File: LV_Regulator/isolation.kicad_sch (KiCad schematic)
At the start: 17 parts, among them IC1 UCC12040DVE, J1 430450800, J2 430450400, J3 430450800, J4 430450400, K1 41.52.9.005.0010, U1 ADM2483xRW

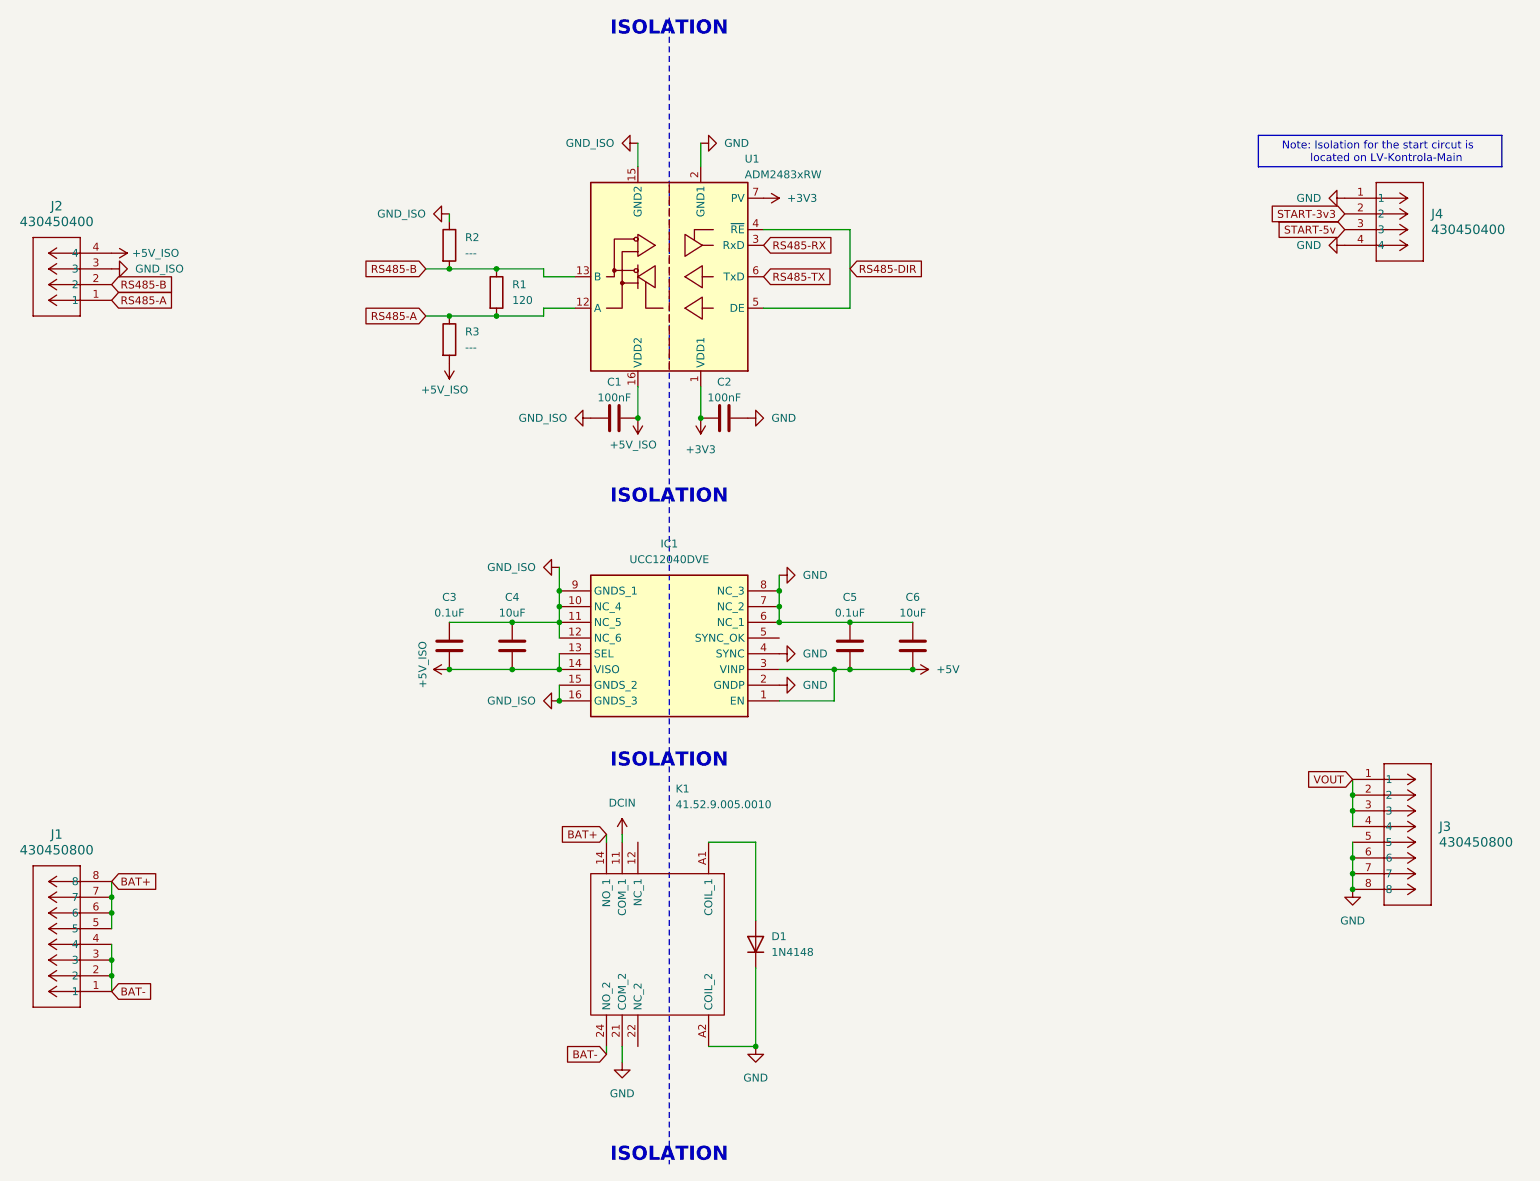
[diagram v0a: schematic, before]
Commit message: Added Start Control
Added Start Control MCU to the LV_Kontrola_Main, added hsc/lsc to LV_Regulator, fixed component numbering
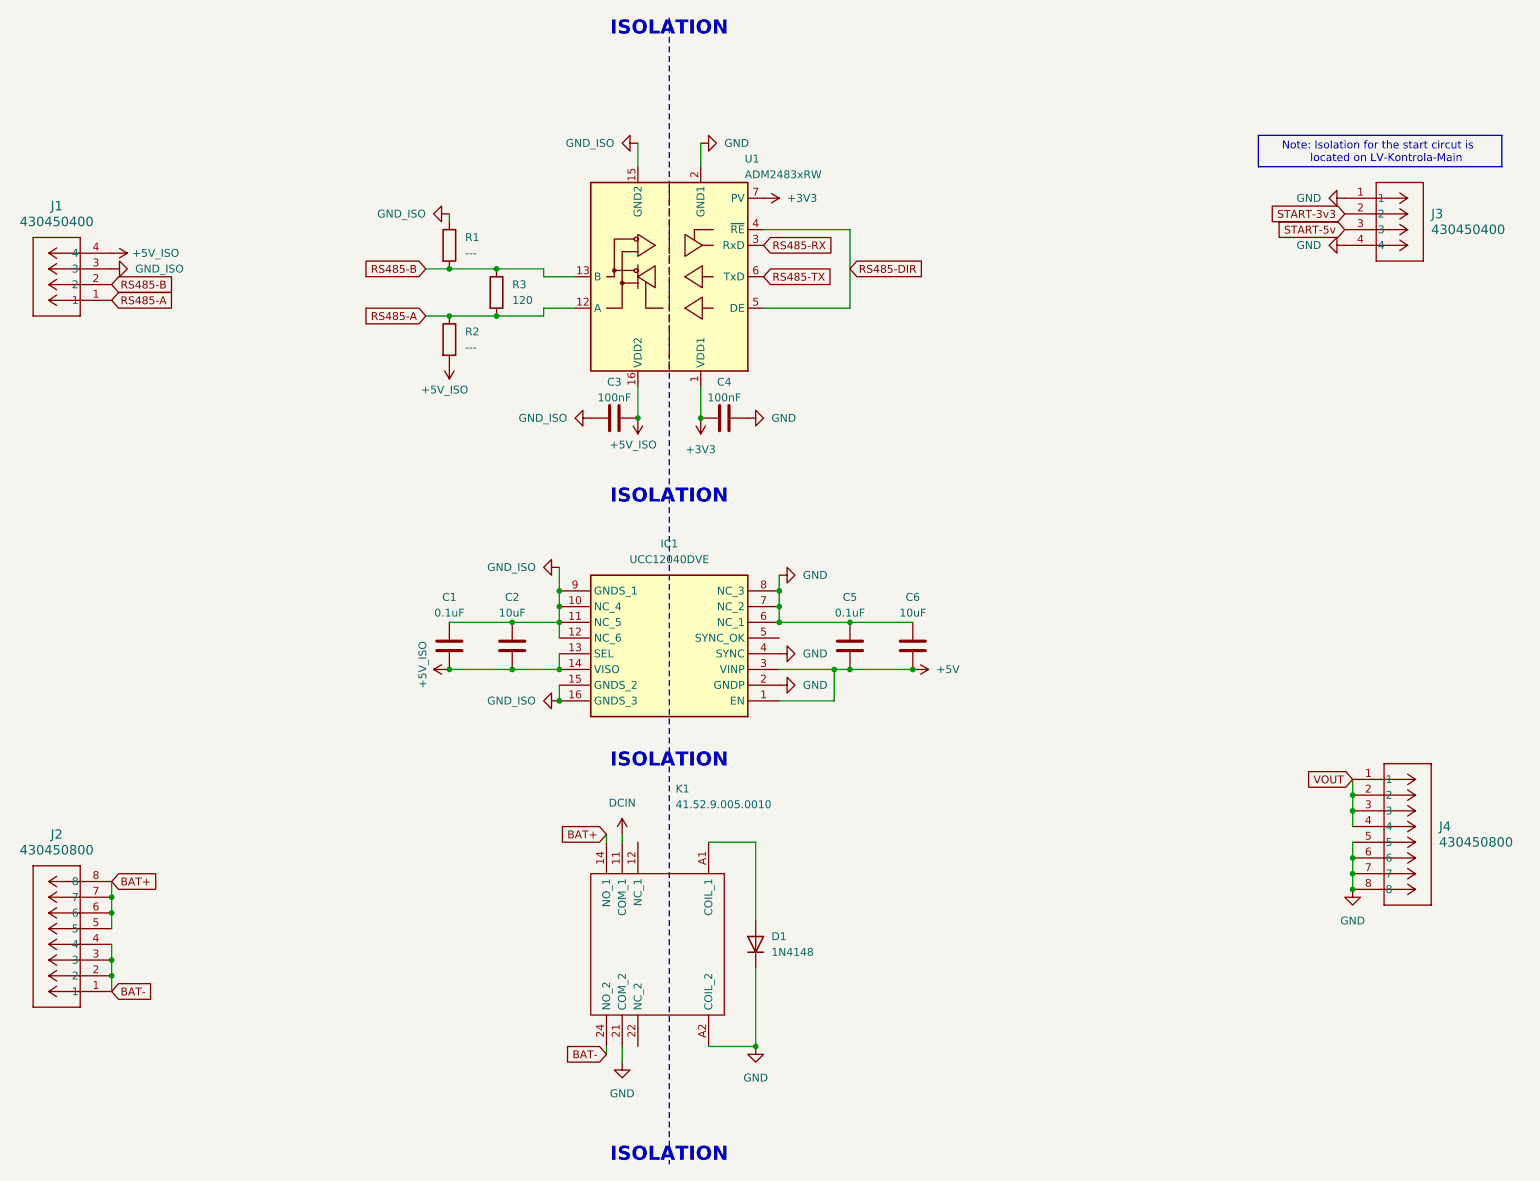
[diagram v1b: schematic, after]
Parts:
- renumbered C3 to C1, C4 to C2, C1 to C3, C2 to C4, J2 to J1, J1 to J2, J4 to J3, J3 to J4, R2 to R1, R3 to R2, R1 to R3

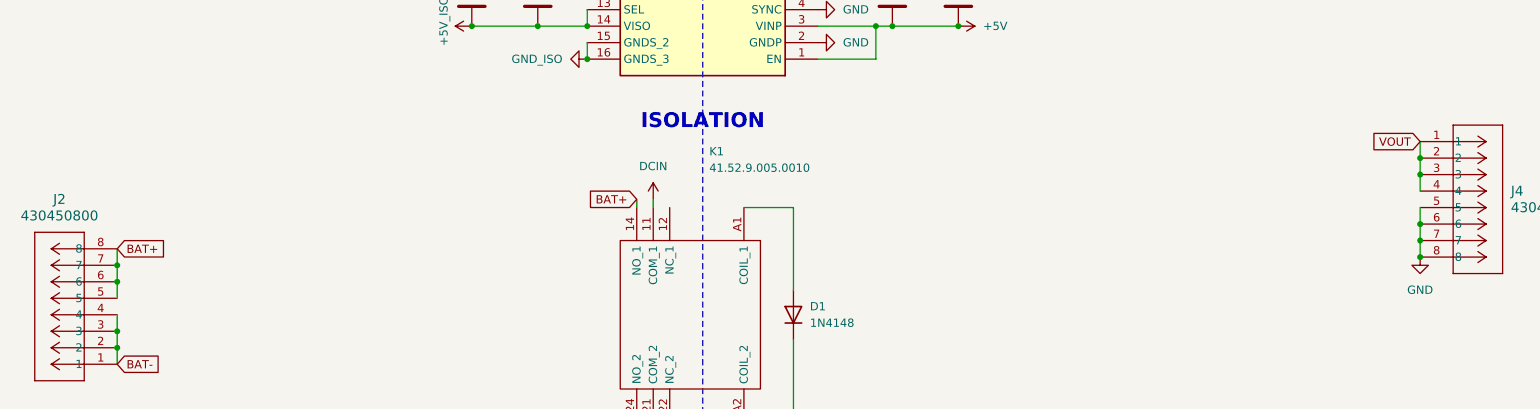
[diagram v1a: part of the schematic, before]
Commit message: Added Stat logic
Added start mcu and associated components to the LV_Kontrola_Main schematic, added STM32CubeIDE project and basic configuration, added fuses to LV_Regulator
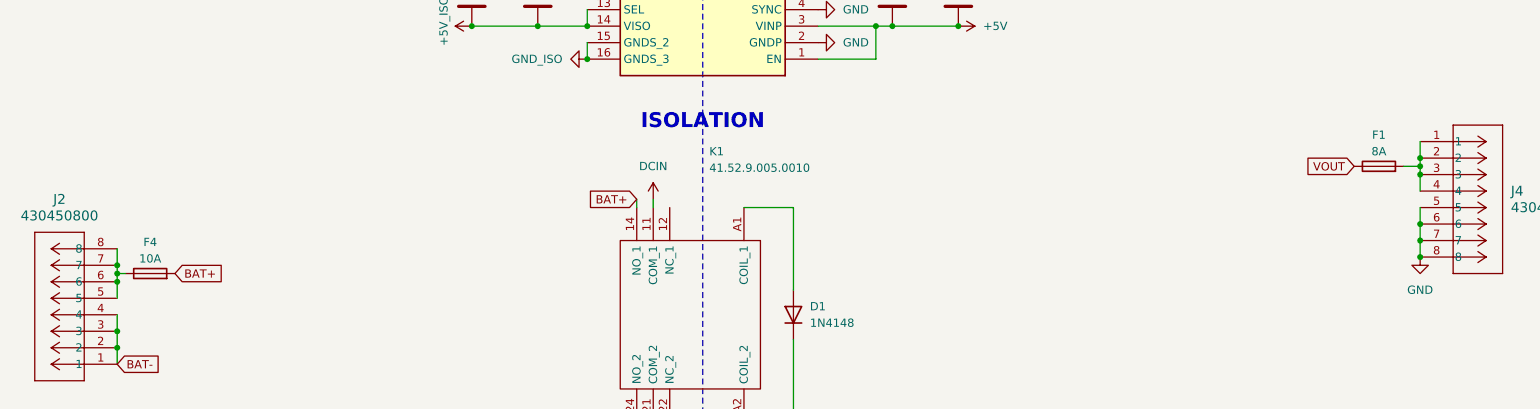
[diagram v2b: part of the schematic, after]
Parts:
- added F1: 8A, symbol Device:Fuse
- added F4: 10A, symbol Device:Fuse
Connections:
- net BAT+: now also F4.2; no longer J2.5, J2.6, J2.7, J2.8
- net VOUT: now also F1.1; no longer J4.1, J4.2, J4.3, J4.4
- new net: F1.2, J4.1, J4.2, J4.3, J4.4
- new net: F4.1, J2.5, J2.6, J2.7, J2.8

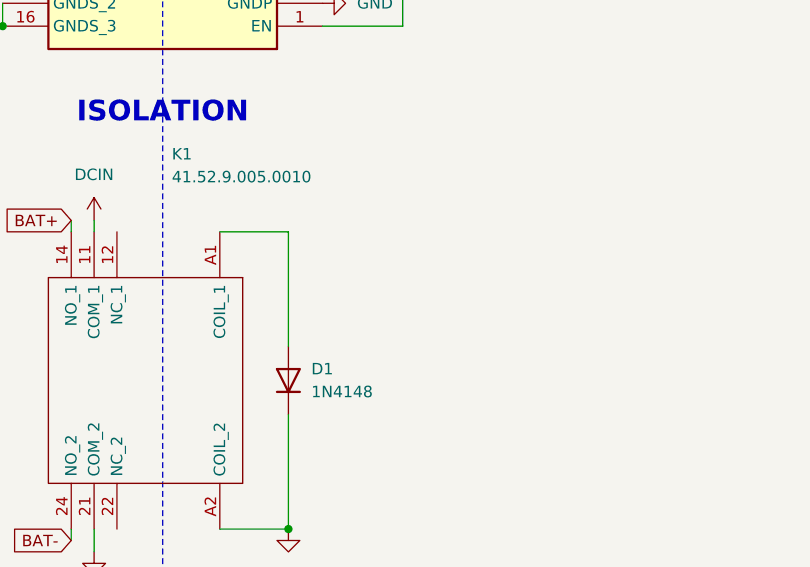
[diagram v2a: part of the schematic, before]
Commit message: LV_Regulator Control changes
Added debug and development equipment, added config. eeprom, more...
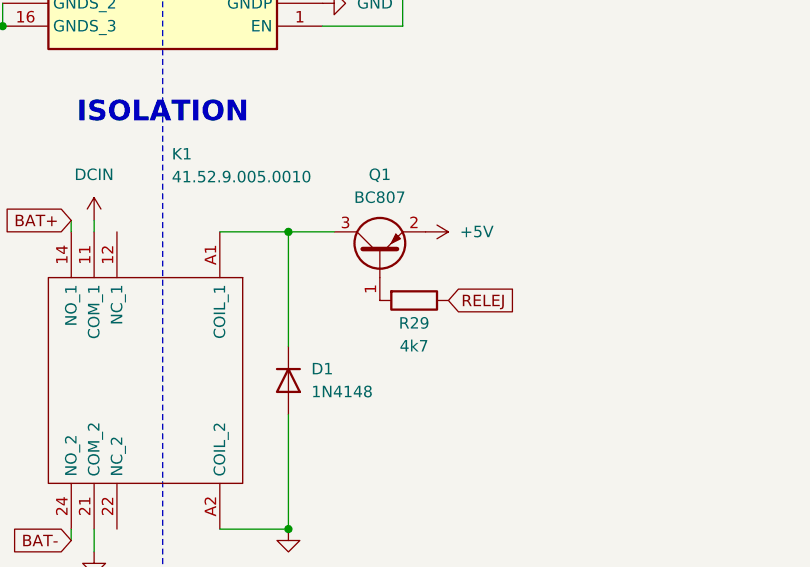
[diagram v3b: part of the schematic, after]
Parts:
- added Q1: BC807, Package_TO_SOT_SMD:SOT-23W_Handsoldering, symbol Transistor_BJT:BC807
- added R29: 4k7, symbol Device:R
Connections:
- net +5V: now also Q1.2 (E)
- net GND: now also D1.2 (A); no longer D1.1 (K)
- net at K1.A1 (COIL_1): now also D1.1 (K), Q1.3 (C); no longer D1.2 (A)
- new net: Q1.1 (B), R29.2
- new net RELEJ: R29.1
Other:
- moved on the sheet: D1

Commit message: Multiple Footprints Added
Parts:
- J1, J3: footprint CONN_SD-43045-001_04_MOL -> microfit-4pin:CONN_SD-43045-001_04_MOL
- J2, J4: footprint CONN_SD-43045-001_08_MOL -> microfit-8pin:CONN_SD-43045-001_08_MOL
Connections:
- no-connect marks 0 -> 3
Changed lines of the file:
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@@
 		(color 0 0 0 0)
 	)
+	(no_connect
+		(at 153.67 113.03)
+	)
+	(no_connect
+		(at 130.81 146.05)
+	)
+	(no_connect
+		(at 130.81 179.07)
+	)
 	(wire
 		(pts
@@
 			)
 		)
-		(property "Footprint" "CONN_SD-43045-001_04_MOL"
+		(property "Footprint" "microfit-4pin:CONN_SD-43045-001_04_MOL"
 			(at 45.72 58.42 0)
 			(effects
@@
 			)
 		)
-		(property "Footprint" "CONN_SD-43045-001_08_MOL"
+		(property "Footprint" "microfit-8pin:CONN_SD-43045-001_08_MOL"
 			(at 45.72 170.18 0)
 			(effects
@@
 			)
 		)
-		(property "Footprint" "CONN_SD-43045-001_04_MOL"
+		(property "Footprint" "microfit-4pin:CONN_SD-43045-001_04_MOL"
 			(at 245.11 41.91 0)
 			(effects
@@
 			)
 		)
-		(property "Footprint" "CONN_SD-43045-001_08_MOL"
+		(property "Footprint" "microfit-8pin:CONN_SD-43045-001_08_MOL"
 			(at 246.38 135.89 0)
 			(effects

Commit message: Added footprints and Test points
Added test points, yet to connect them have to find where they all go exactly
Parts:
- R1, R2, R29, R3: footprint (none) -> Resistor_SMD:R_1206_3216Metric_Pad1.30x1.75mm_HandSolder
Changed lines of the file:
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@@
 			)
 		)
-		(property "Footprint" ""
+		(property "Footprint" "Resistor_SMD:R_1206_3216Metric_Pad1.30x1.75mm_HandSolder"
 			(at 163.83 151.892 90)
 			(effects
@@
 			)
 		)
-		(property "Footprint" ""
+		(property "Footprint" "Resistor_SMD:R_1206_3216Metric_Pad1.30x1.75mm_HandSolder"
 			(at 98.552 49.53 90)
 			(effects
@@
 			)
 		)
-		(property "Footprint" ""
+		(property "Footprint" "Resistor_SMD:R_1206_3216Metric_Pad1.30x1.75mm_HandSolder"
 			(at 98.552 64.77 90)
 			(effects
@@
 			)
 		)
-		(property "Footprint" ""
+		(property "Footprint" "Resistor_SMD:R_1206_3216Metric_Pad1.30x1.75mm_HandSolder"
 			(at 106.172 57.15 90)
 			(effects

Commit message: Added Footprints & Links for Component Purchase
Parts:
- C1, C5: footprint (none) -> Capacitor_SMD:C_1206_3216Metric_Pad1.33x1.80mm_HandSolder; Purchase Place (none) -> http://eu.mouser.com/ProductDetail/KYOCERA-AVX/12066D104KAT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
- C2: footprint (none) -> Capacitor_SMD:C_1206_3216Metric_Pad1.33x1.80mm_HandSolder; Field5 (none) -> https://eu.mouser.com/ProductDetail/Samsung-Electro-Mechani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
- C3, C4: footprint (none) -> Capacitor_SMD:C_1206_3216Metric_Pad1.33x1.80mm_HandSolder; Purchase Place (none) -> https://eu.mouser.com/ProductDetail/KEMET/C1206Y104K9RACTU?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
- C6: footprint (none) -> Capacitor_SMD:C_1206_3216Metric_Pad1.33x1.80mm_HandSolder; Purchase Place (none) -> https://eu.mouser.com/ProductDetail/Samsung-Electro-Mechani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
- D1: footprint (none) -> Diode_SMD:D_1206_3216Metric_Pad1.42x1.75mm_HandSolder; Purchase Place (none) -> https://www.mgelectronic.rs/dioda-1n4148-1206
- F1: footprint (none) -> Fuse:Fuse_1206_3216Metric_Pad1.42x1.75mm_HandSolder; Purchase Place (none) -> https://eu.mouser.com/ProductDetail/YAGEO/JB12S8001R?qs=iLK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
- F4: footprint (none) -> Fuse:Fuse_1206_3216Metric_Pad1.42x1.75mm_HandSolder; Purchase Place (none) -> https://eu.mouser.com/ProductDetail/YAGEO/JB12F1002R?qs=iLK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
- IC1: footprint SOIC127P1030X265-16N -> LIB_UCC12040DVE:SOIC127P1030X265-16N
- K1: footprint 415290050010 -> LIB_41.52.9.005.0010:415290050010
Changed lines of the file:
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@@
 			)
 		)
-		(property "Footprint" ""
+		(property "Footprint" "Capacitor_SMD:C_1206_3216Metric_Pad1.33x1.80mm_HandSolder"
 			(at 99.3648 110.49 0)
 			(effects
@@
 			)
 		)
+		(property "Purchase Place" "http://eu.mouser.com/ProductDetail/KYOCERA-AVX/12066D104KAT4A?qs=sGAEpiMZZMsh%252B1woXyUXj0xLsiAJ%252BgLBdVdBYBTQiUU%3D"
+			(at 100.33 114.3 0)
+			(effects
+				(font
+					(size 1.27 1.27)
+				)
+				(hide yes)
+			)
+		)
 		(pin "1"
 		)
@@
 			)
 		)
-		(property "Footprint" ""
+		(property "Footprint" "Capacitor_SMD:C_1206_3216Metric_Pad1.33x1.80mm_HandSolder"
 			(at 174.2948 110.49 0)
 			(effects
@@
 		)
 		(property "Description" "Unpolarized capacitor"
+			(at 175.26 114.3 0)
+			(effects
+				(font
+					(size 1.27 1.27)
+				)
+				(hide yes)
+			)
+		)
+		(property "Purchase Place" "https://eu.mouser.com/ProductDetail/Samsung-Electro-Mechanics/CL31A106KQHNNWE?qs=X6jEic%2FHinDPxVHbcNEesg%3D%3D"
 			(at 175.26 114.3 0)
 			(effects
@@
 			)
 		)
-		(property "Footprint" "415290050010"
+		(property "Footprint" "LIB_41.52.9.005.0010:415290050010"
 			(at 135.382 175.26 0)
 			(effects
@@
 			)
 		)
-		(property "Footprint" ""
+		(property "Footprint" "Fuse:Fuse_1206_3216Metric_Pad1.42x1.75mm_HandSolder"
 			(at 240.03 141.478 90)
 			(effects
@@
 		(property "Description" "Fuse"
 			(at 240.03 139.7 0)
+			(effects
+				(font
+					(size 1.27 1.27)
+				)
+				(hide yes)
+			)
+		)
+		(property "Purchase Place" "https://eu.mouser.com/ProductDetail/YAGEO/JB12S8001R?qs=iLKYxzqNS74e9XUtVrcPUA%3D%3D"
+			(at 240.03 139.7 90)
 			(effects
 				(font
@@
 			)
 		)
-		(property "Footprint" ""
+		(property "Footprint" "Capacitor_SMD:C_1206_3216Metric_Pad1.33x1.80mm_HandSolder"
 			(at 130.81 76.5048 0)
 			(effects
@@
 			)
 		)
+		(property "Purchase Place" "https://eu.mouser.com/ProductDetail/KEMET/C1206Y104K9RACTU?qs=rUPLZ6nenJPIO9Oy%2FdArjw%3D%3D"
+			(at 127 77.47 90)
+			(effects
+				(font
+					(size 1.27 1.27)
+				)
+				(hide yes)
+			)
+		)
 		(pin "1"
 		)
@@
 			)
 		)
-		(property "Footprint" ""
+		(property "Footprint" "Capacitor_SMD:C_1206_3216Metric_Pad1.33x1.80mm_HandSolder"
 			(at 109.5248 110.49 0)
 			(effects
@@
 		)
 		(property "Description" "Unpolarized capacitor"
+			(at 110.49 114.3 0)
+			(effects
+				(font
+					(size 1.27 1.27)
+				)
+				(hide yes)
+			)
+		)
+		(property "Field5" "https://eu.mouser.com/ProductDetail/Samsung-Electro-Mechanics/CL31A106KQHNNWE?qs=X6jEic%2FHinDPxVHbcNEesg%3D%3D"
 			(at 110.49 114.3 0)
 			(effects
@@
 			)
 		)
-		(property "Footprint" ""
+		(property "Footprint" "Fuse:Fuse_1206_3216Metric_Pad1.42x1.75mm_HandSolder"
 			(at 50.8 157.988 90)
 			(effects
@@
 		(property "Description" "Fuse"
 			(at 50.8 156.21 0)
+			(effects
+				(font
+					(size 1.27 1.27)
+				)
+				(hide yes)
+			)
+		)
+		(property "Purchase Place" "https://eu.mouser.com/ProductDetail/YAGEO/JB12F1002R?qs=iLKYxzqNS77quI8BrLxxaw%3D%3D"
+			(at 50.8 156.21 90)
 			(effects
 				(font
@@
 			)
 		)
-		(property "Footprint" ""
+		(property "Footprint" "Capacitor_SMD:C_1206_3216Metric_Pad1.33x1.80mm_HandSolder"
 			(at 148.59 76.5048 0)
 			(effects
@@
 		(property "Description" "Unpolarized capacitor"
 			(at 144.78 77.47 0)
+			(effects
+				(font
+					(size 1.27 1.27)
+				)
+				(hide yes)
+			)
+		)
+		(property "Purchase Place" "https://eu.mouser.com/ProductDetail/KEMET/C1206Y104K9RACTU?qs=rUPLZ6nenJPIO9Oy%2FdArjw%3D%3D"
+			(at 144.78 77.47 90)
 			(effects
 				(font
@@
 			)
 		)
-		(property "Footprint" ""
+		(property "Footprint" "Capacitor_SMD:C_1206_3216Metric_Pad1.33x1.80mm_HandSolder"
 			(at 164.1348 110.49 0)
 			(effects
@@
 		)
 		(property "Description" "Unpolarized capacitor"
+			(at 165.1 114.3 0)
+			(effects
+				(font
+					(size 1.27 1.27)
+				)
+				(hide yes)
+			)
+		)
+		(property "Purchase Place" "http://eu.mouser.com/ProductDetail/KYOCERA-AVX/12066D104KAT4A?qs=sGAEpiMZZMsh%252B1woXyUXj0xLsiAJ%252BgLBdVdBYBTQiUU%3D"
 			(at 165.1 114.3 0)
 			(effects
@@
 			)
 		)
-		(property "Footprint" "SOIC127P1030X265-16N"
+		(property "Footprint" "LIB_UCC12040DVE:SOIC127P1030X265-16N"
 			(at 121.92 28.27 0)
 			(effects
@@
 			)
 		)
-		(property "Footprint" ""
+		(property "Footprint" "Diode_SMD:D_1206_3216Metric_Pad1.42x1.75mm_HandSolder"
 			(at 149.86 162.56 0)
 			(effects
@@
 			(effects
 				(font
+					(size 1.27 1.27)
+				)
+				(hide yes)
+			)
+		)
+		(property "Purchase Place" "https://www.mgelectronic.rs/dioda-1n4148-1206"
+			(at 149.86 162.56 90)
+			(effects
+				(font
